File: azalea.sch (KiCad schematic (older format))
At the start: 103 parts, among them J1 NEIGHBOR1, J2 NEIGHBOR2, J3 USB-MICRO-B-SHIELDED, J4 USB-MICRO-B-SHIELDED, J5 JTAG, J6 POWER, J7 BONUS_ROW, SW1 DFU, SW2 RESET, U1 LPC4330FBD144, U2 W25Q16DV, U3 AP7333, U4 IP4220CZ6, U5 AP2553W6-7, X1 MCU_XTAL, X2 RTC_XTAL

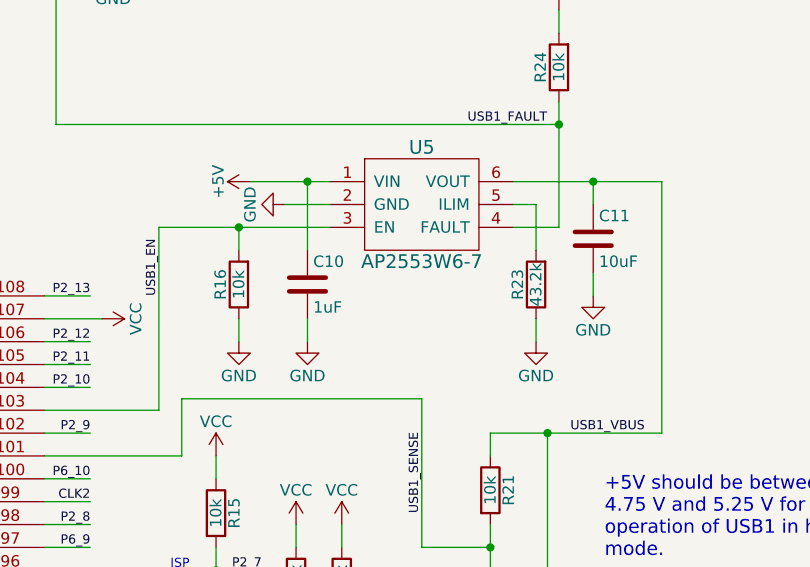
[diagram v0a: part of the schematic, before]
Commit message: GF1 hardware: Update U5 & R23 with AP22653AW6-7 p/n and res value.
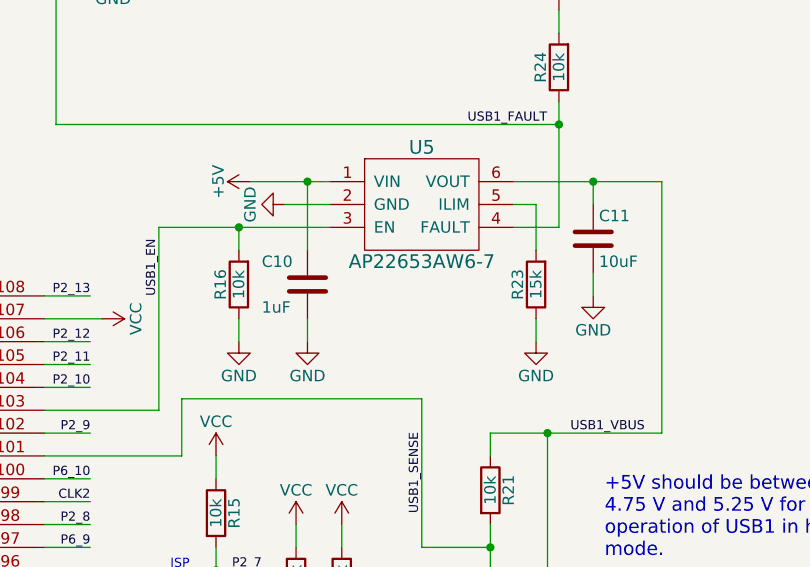
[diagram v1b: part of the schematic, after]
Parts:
- R23: value 43.2k -> 15k; Description RES SMD 43.2K OHM 1% 1/10W 0603 -> RES SMD 15K OHM 5% 1/10W 0603; Part Number RC0603FR-0743K2L -> RC0603JR-0715KL
- U5: value AP2553W6-7 -> AP22653AW6-7; Part Number AP2553W6-7 -> AP22653AW6-7
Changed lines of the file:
@@
 U 1 1 56009D0E
 P 12400 3550
-F 0 "C10" H 12425 3650 50  0000 L CNN
-F 1 "1uF" H 12425 3450 50  0000 L CNN
+F 0 "C10" H 12200 3650 50  0000 L CNN
+F 1 "1uF" H 12200 3450 50  0000 L CNN
 F 2 "gsg-modules:0603" H 12438 3400 30  0001 C CNN
 F 3 "" H 12400 3550 60  0000 C CNN
@@
 P 12900 3200
 F 0 "U5" H 12900 3450 60  0000 C CNN
-F 1 "AP2553W6-7" H 12900 2950 60  0000 C CNN
+F 1 "AP22653AW6-7" H 12900 2950 60  0000 C CNN
 F 2 "gsg-modules:SOT457" H 12900 3200 60  0001 C CNN
 F 3 "" H 12900 3200 60  0000 C CNN
 F 4 "Diodes Inc." H 12900 3200 60  0001 C CNN "Manufacturer"
-F 5 "AP2553W6-7" H 12900 3200 60  0001 C CNN "Part Number"
+F 5 "AP22653AW6-7" H 12900 3200 60  0001 C CNN "Part Number"
 F 6 "IC PD SW CURR LIMIT SOT26 " H 12900 3200 60  0001 C CNN "Description"
 	1    12900 3200
@@
 P 13400 3550
 F 0 "R23" V 13480 3550 50  0000 C CNN
-F 1 "43.2k" V 13400 3550 50  0000 C CNN
+F 1 "15k" V 13400 3550 50  0000 C CNN
 F 2 "gsg-modules:0603" V 13330 3550 30  0001 C CNN
 F 3 "" H 13400 3550 30  0000 C CNN
 F 4 "Yageo" H 13400 3550 60  0001 C CNN "Manufacturer"
-F 5 "RC0603FR-0743K2L" H 13400 3550 60  0001 C CNN "Part Number"
-F 6 "RES SMD 43.2K OHM 1% 1/10W 0603 " H 13400 3550 60  0001 C CNN "Description"
+F 5 "RC0603JR-0715KL" H 13400 3550 60  0001 C CNN "Part Number"
+F 6 "RES SMD 15K OHM 5% 1/10W 0603" H 13400 3550 50  0001 C CNN "Description"
 	1    13400 3550
 	-1   0    0    1

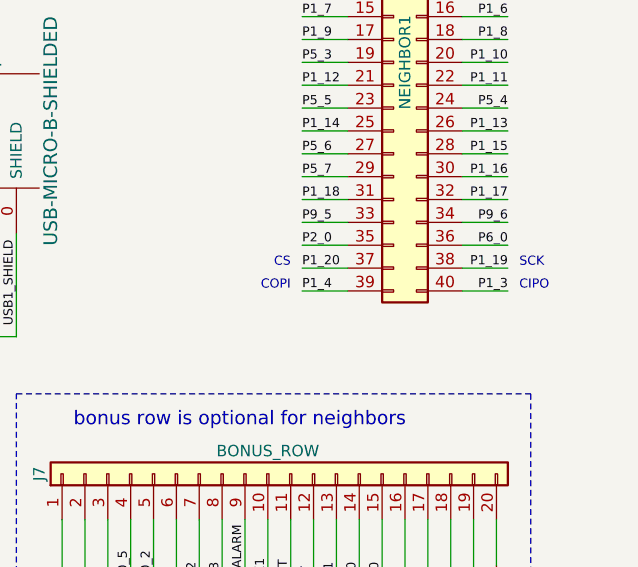
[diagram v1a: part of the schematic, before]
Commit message: GF1 hardware: Update references from MOSI/MISO or COPI/CIPO to PICO/POCI
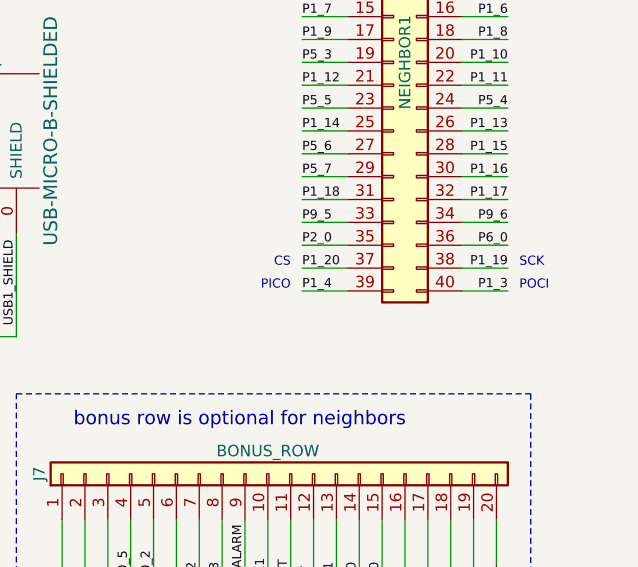
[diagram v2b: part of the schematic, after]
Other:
- note added: "PICO"
- note added: "POCI"
- note removed: "CIPO"
- note removed: "COPI"
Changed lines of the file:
@@
 Sheet 1 1
 Title "Azalea"
-Date "2021-11-23"
+Date "2021-12-02"
 Rev ""
 Comp "Copyright 2015-2021 Great Scott Gadgets"
@@
 P2_0
 Text Notes 16250 6200 0    40   ~ 0
-CIPO
+POCI
 Text Notes 15250 6200 2    40   ~ 0
-COPI
+PICO
 Text Notes 16250 6100 0    40   ~ 0
 SCK
